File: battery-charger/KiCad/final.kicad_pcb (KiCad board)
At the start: 2 copper layers, 100 x 23 mm, 20 parts, among them P1 CONN_01X03, Q1 MOSFET_P, SW1 SPST, U1 BQ2057W

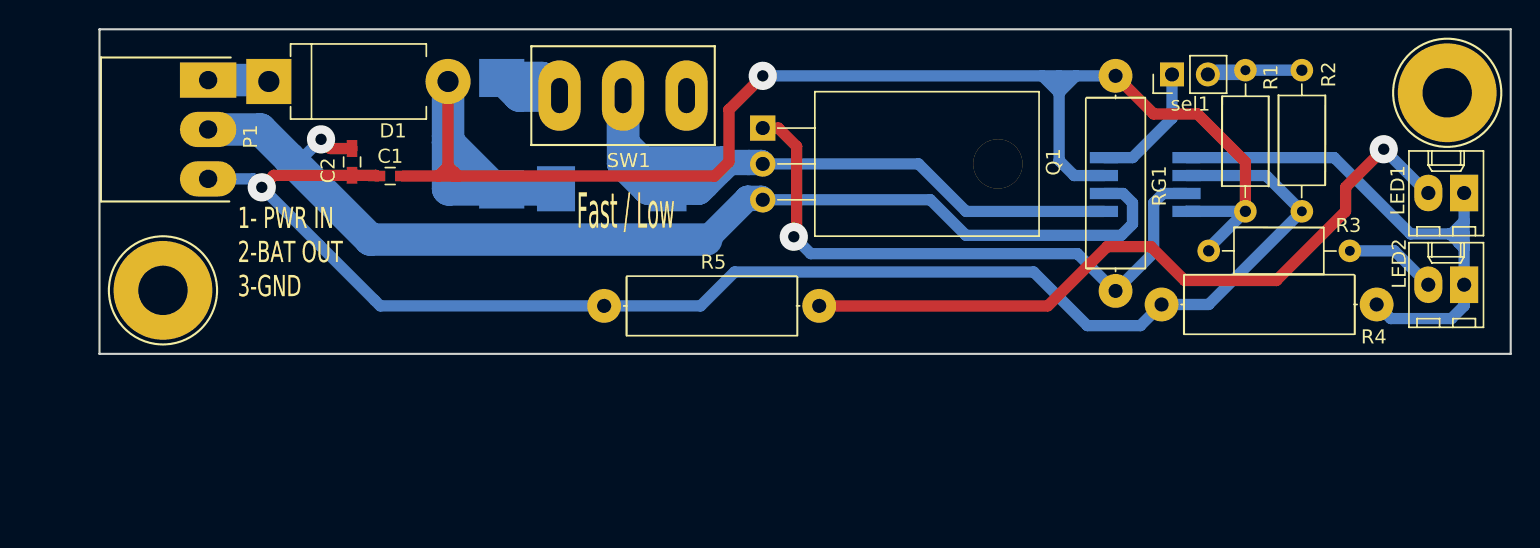
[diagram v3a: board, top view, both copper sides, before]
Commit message: Fix some errors in the border of boards to panelize them correctly
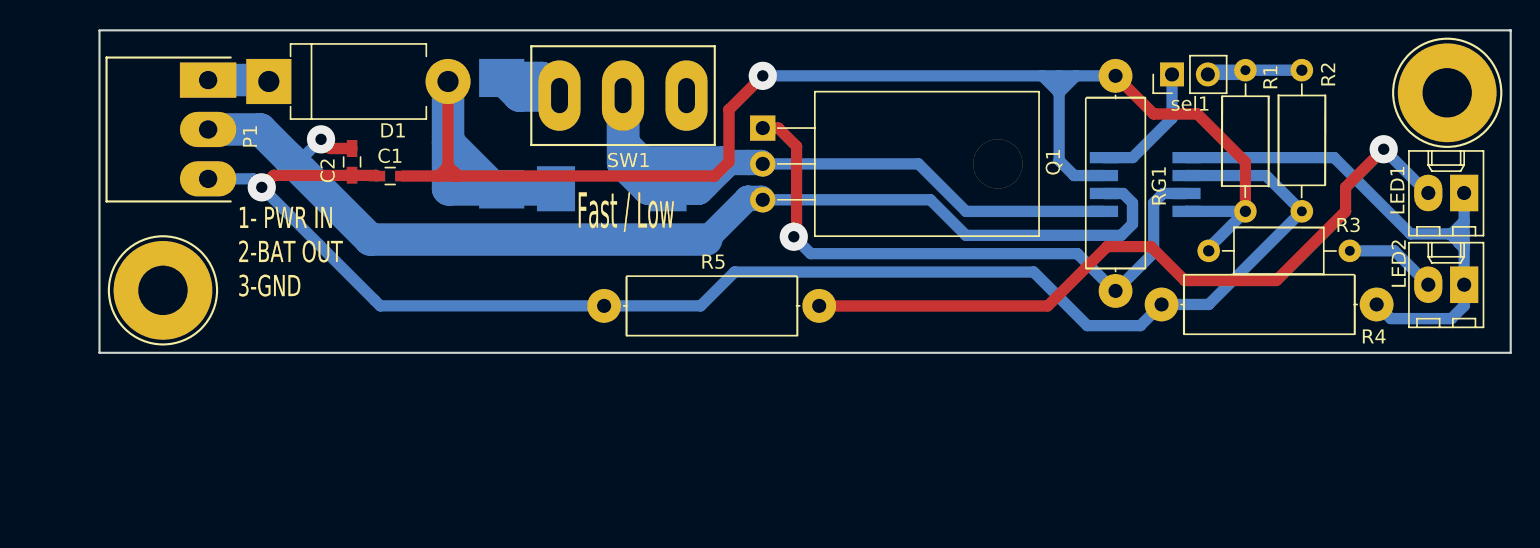
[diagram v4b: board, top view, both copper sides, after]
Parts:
- P1: footprint footprint:Molex_03x01_Straight -> Molex_03x01_Straight
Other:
- board size 100 x 23 mm -> 100 x 22.8 mm
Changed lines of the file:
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@@
     (links 32)
     (no_connects 0)
-    (area 99.924999 79.924999 200.075001 103.075001)
+    (area 91.922621 73.925 206.934525 105.429)
     (thickness 1.6)
-    (drawings 24)
+    (drawings 28)
     (tracks 161)
     (zones 0)
@@
     (pad_drill 0.6)
     (pad_to_mask_clearance 0.1)
-    (aux_axis_origin 0 0)
+    (aux_axis_origin 99.925 103.075)
     (visible_elements 7FFEDE69)
     (pcbplotparams
@@
     (uvia_dia 1.2)
     (uvia_drill 0.6)
+  )
+  (module Molex_03x01_Straight (layer F.Cu)
+    (at 104.7 86.6 270)
+    (descr "Connector Headers with Friction Lock, 26-60-4020, http://www.molex.com/pdm_docs/sd/026604020_sd.pdf")
+    (tags "connector molex kk_41791 26-60-4020")
+    (fp_text reference P1 (at 1 -6 270) (layer F.SilkS)
+      (effects (font (size 1 1) (thickness 0.15)))
+    )
+    (fp_text value CONN_01X03 (at 0.5 7 270) (layer F.Fab)
+      (effects (font (size 1 1) (thickness 0.15)))
+    )
+    (fp_line (start -4.6 4.2) (end -4.6 -4.6) (layer F.SilkS) (width 0.15))
+    (fp_line (start 5.6 4.2) (end 5.6 -4.6) (layer F.SilkS) (width 0.15))
+    (fp_line (start 6.1 -4.9) (end 6.1 5) (layer F.CrtYd) (width 0.15))
+    (fp_line (start 6.2 5.1) (end -5 5.1) (layer F.CrtYd) (width 0.15))
+    (fp_line (start -5 5.1) (end -5 -4.9) (layer F.CrtYd) (width 0.15))
+    (fp_line (start 5.6 4.2) (end -4.6 4.2) (layer F.SilkS) (width 0.15))
+    (fp_line (start -4.5 4.5) (end 5.5 4.5) (layer F.Fab) (width 0.15))
+    (fp_line (start 5.5 4.5) (end 5.5 -4.5) (layer F.Fab) (width 0.15))
+    (fp_line (start -4.5 -4.5) (end -4.5 4.5) (layer F.Fab) (width 0.15))
+    (fp_text user %R (at 0.8 1.3 270) (layer F.Fab)
+      (effects (font (size 1 1) (thickness 0.15)))
+    )
+    (pad 1 thru_hole rect (at -3 -3 270) (size 2.5 4) (drill 1.3) (layers *.Cu *.Mask)
+      (net 4 /PWR_IN))
+    (pad 2 thru_hole oval (at 0.5 -3 270) (size 2.5 4) (drill 1.3) (layers *.Cu *.Mask)
+      (net 3 /BAT_OUT))
+    (pad 3 thru_hole oval (at 4 -3 270) (size 2.5 4) (drill 1.3) (layers *.Cu *.Mask)
+      (net 2 /GND))
   )
   (module footprint:C_0603 (layer F.Cu)
@@
     )
   )
-  (module footprint:Molex_03x01_Straight (layer F.Cu)
-    (at 104.7 86.6 270)
-    (descr "Connector Headers with Friction Lock, 26-60-4020, http://www.molex.com/pdm_docs/sd/026604020_sd.pdf")
-    (tags "connector molex kk_41791 26-60-4020")
-    (fp_text reference P1 (at 1 -6 270) (layer F.SilkS)
-      (effects (font (size 1 1) (thickness 0.15)))
-    )
-    (fp_text value CONN_01X03 (at 0.5 7 270) (layer F.Fab)
-      (effects (font (size 1 1) (thickness 0.15)))
-    )
-    (fp_line (start 6.1 -4.9) (end 6.1 5) (layer F.CrtYd) (width 0.15))
-    (fp_line (start 6.2 5.1) (end -5 5.1) (layer F.CrtYd) (width 0.15))
-    (fp_line (start -5 5.1) (end -5 -4.9) (layer F.CrtYd) (width 0.15))
-    (fp_line (start 5.6 -4.5) (end 5.6 4.6) (layer F.SilkS) (width 0.15))
-    (fp_line (start 5.6 4.6) (end -4.6 4.6) (layer F.SilkS) (width 0.15))
-    (fp_line (start -4.6 4.6) (end -4.6 -4.6) (layer F.SilkS) (width 0.15))
-    (fp_line (start -4.5 4.5) (end 5.5 4.5) (layer F.Fab) (width 0.15))
-    (fp_line (start 5.5 4.5) (end 5.5 -4.5) (layer F.Fab) (width 0.15))
-    (fp_line (start -4.5 -4.5) (end -4.5 4.5) (layer F.Fab) (width 0.15))
-    (fp_text user %R (at 0.8 1.3 270) (layer F.Fab)
-      (effects (font (size 1 1) (thickness 0.15)))
-    )
-    (pad 1 thru_hole rect (at -3 -3 270) (size 2.5 4) (drill 1.3) (layers *.Cu *.Mask)
-      (net 4 /PWR_IN))
-    (pad 2 thru_hole oval (at 0.5 -3 270) (size 2.5 4) (drill 1.3) (layers *.Cu *.Mask)
-      (net 3 /BAT_OUT))
-    (pad 3 thru_hole oval (at 4 -3 270) (size 2.5 4) (drill 1.3) (layers *.Cu *.Mask)
-      (net 2 /GND))
-  )
   (module footprint:Mounting_hole (layer F.Cu)
     (at 104.5 98.5)
@@
       (rotate (xyz 0 0 0))
     )
+  )
+  (gr_line (start 100 102.92) (end 100 80.1) (angle 90) (layer Edge.Cuts) (width 0.15))
+  (gr_line (start 200 80.08) (end 199.97 80.08) (angle 90) (layer Edge.Cuts) (width 0.15))
+  (gr_line (start 200 102.92) (end 200 80.08) (angle 90) (layer Edge.Cuts) (width 0.15))
+  (dimension 0.15 (width 0.25) (layer Margin)
+    (gr_text 0,150mm (at 77.62 80.005 90) (layer Margin)
+      (effects (font (size 1 1) (thickness 0.25)))
+    )
+    (feature1 (pts (xy 101.99 79.93) (xy 76.62 79.93)))
+    (feature2 (pts (xy 101.99 80.08) (xy 76.62 80.08)))
+    (crossbar (pts (xy 78.62 80.08) (xy 78.62 79.93)))
+    (arrow1a (pts (xy 78.62 79.93) (xy 79.206421 81.056504)))
+    (arrow1b (pts (xy 78.62 79.93) (xy 78.033579 81.056504)))
+    (arrow2a (pts (xy 78.62 80.08) (xy 79.206421 78.953496)))
+    (arrow2b (pts (xy 78.62 80.08) (xy 78.033579 78.953496)))
+  )
+  (dimension 23.15 (width 0.25) (layer Margin)
+    (gr_text 23,150mm (at 83.72 91.505 90) (layer Margin)
+      (effects (font (size 1 1) (thickness 0.25)))
+    )
+    (feature1 (pts (xy 100.08 79.93) (xy 82.72 79.93)))
+    (feature2 (pts (xy 100.08 103.08) (xy 82.72 103.08)))
+    (crossbar (pts (xy 84.72 103.08) (xy 84.72 79.93)))
+    (arrow1a (pts (xy 84.72 79.93) (xy 85.306421 81.056504)))
+    (arrow1b (pts (xy 84.72 79.93) (xy 84.133579 81.056504)))
+    (arrow2a (pts (xy 84.72 103.08) (xy 85.306421 101.953496)))
+    (arrow2b (pts (xy 84.72 103.08) (xy 84.133579 101.953496)))
+  )
+  (dimension 23.160019 (width 0.25) (layer Margin)
+    (gr_text 23,160mm (at 92.068589 91.489615 89.92578271) (layer Margin)
+      (effects (font (size 1 1) (thickness 0.25)))
+    )
+    (feature1 (pts (xy 100.1 79.92) (xy 91.08359 79.90832)))
+    (feature2 (pts (xy 100.07 103.08) (xy 91.05359 103.06832)))
+    (crossbar (pts (xy 93.053588 103.070911) (xy 93.083588 79.910911)))
+    (arrow1a (pts (xy 93.083588 79.910911) (xy 93.668549 81.038173)))
+    (arrow1b (pts (xy 93.083588 79.910911) (xy 92.495709 81.036654)))
+    (arrow2a (pts (xy 93.053588 103.070911) (xy 93.641467 101.945168)))
+    (arrow2b (pts (xy 93.053588 103.070911) (xy 92.468627 101.943649)))
   )
   (gr_text "1- PWR IN\n2-BAT OUT\n3-GND" (at 109.8 95.8) (layer F.SilkS)
@@
     (arrow2b (pts (xy 198 78) (xy 199.126504 77.413579)))
   )
-  (gr_line (start 100 103) (end 100 80) (angle 90) (layer Edge.Cuts) (width 0.15))
-  (gr_line (start 200 103) (end 100 103) (angle 90) (layer Edge.Cuts) (width 0.15))
-  (gr_line (start 200 80) (end 200 103) (angle 90) (layer Edge.Cuts) (width 0.15))
-  (gr_line (start 100 80) (end 200 80) (angle 90) (layer Edge.Cuts) (width 0.15))
+  (gr_line (start 200 102.925) (end 100 102.925) (angle 90) (layer Edge.Cuts) (width 0.15))
+  (gr_line (start 100 80.075) (end 200 80.075) (angle 90) (layer Edge.Cuts) (width 0.15))
   (segment (start 178.6 95.7) (end 178.6 95.5) (width 0.8) (layer B.Cu) (net 1))
   (segment (start 178.6 95.5) (end 181.2 92.9) (width 0.8) (layer B.Cu) (net 1))
